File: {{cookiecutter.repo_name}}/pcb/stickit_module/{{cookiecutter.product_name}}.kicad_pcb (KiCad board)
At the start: 2 copper layers, 49.5 x 20.3 mm, 13 parts

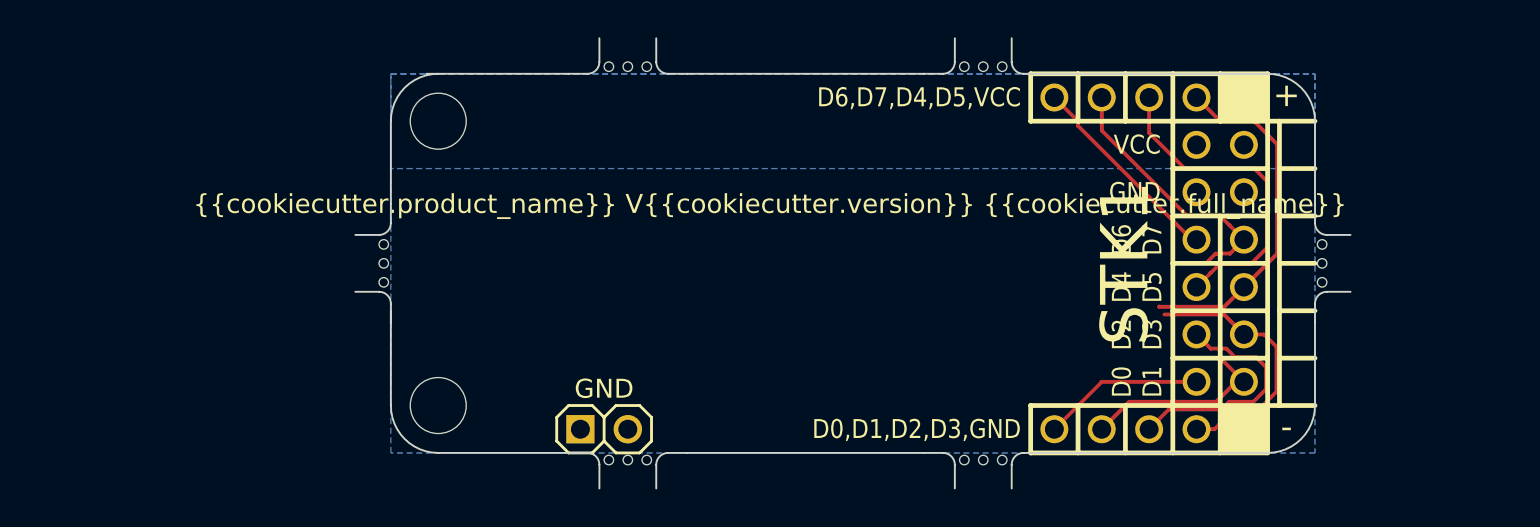
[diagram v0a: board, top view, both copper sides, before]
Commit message: Added VCC access point to StickIt! module template. * Added template for RPi HAT. * Added template for StickIt! motherboard.
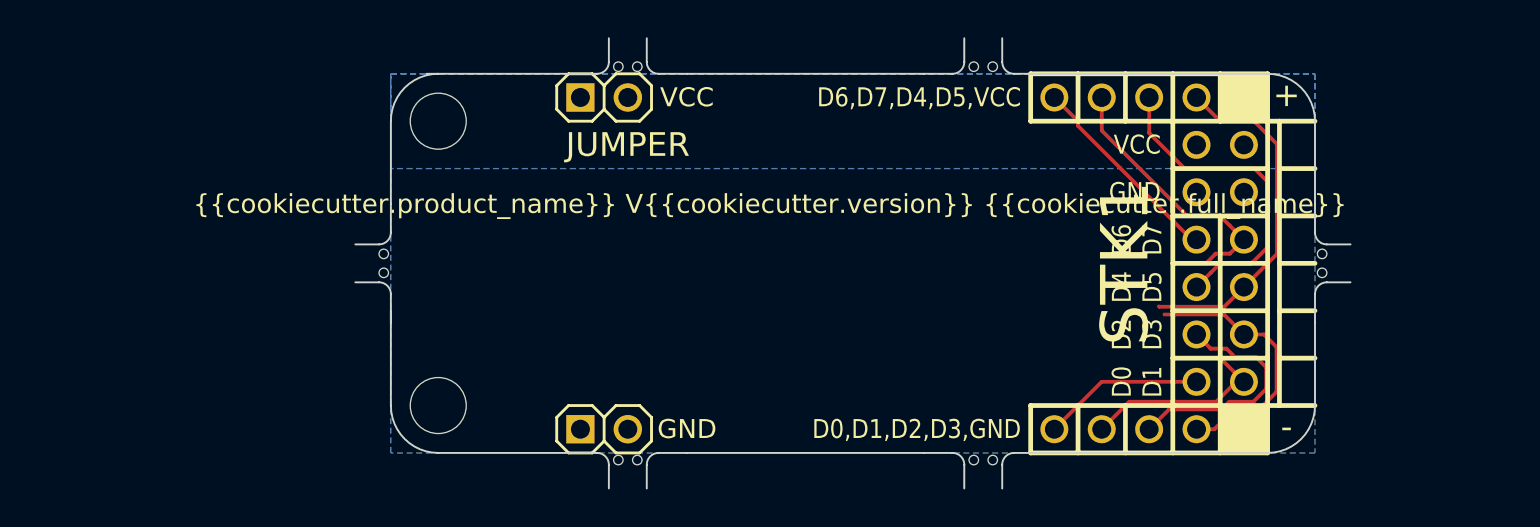
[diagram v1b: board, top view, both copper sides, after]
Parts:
- added JP2: JUMPER, XESS:HDR_1x2, F.Cu at (11.4, 1.27)
- JP1: value (none) -> JUMPER
- Ref** (x6): footprint XESS:Array_Tab_Null -> XESS:Array_Tab_2hole
